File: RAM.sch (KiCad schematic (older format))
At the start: 33 parts, among them IC1 EP4CE10F17, U22 W9751G6KB

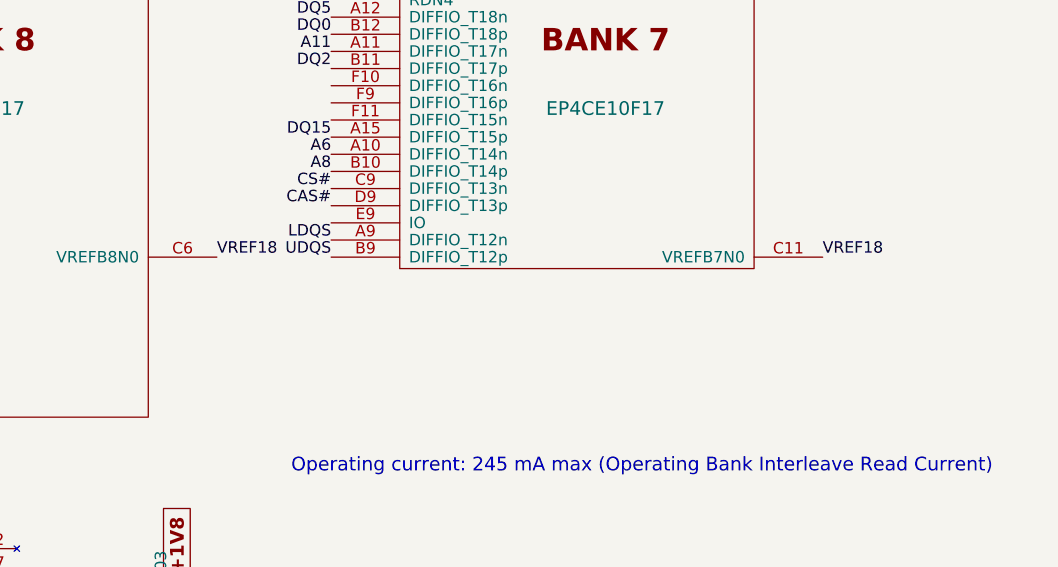
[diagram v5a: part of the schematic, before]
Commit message: More caps for VREF
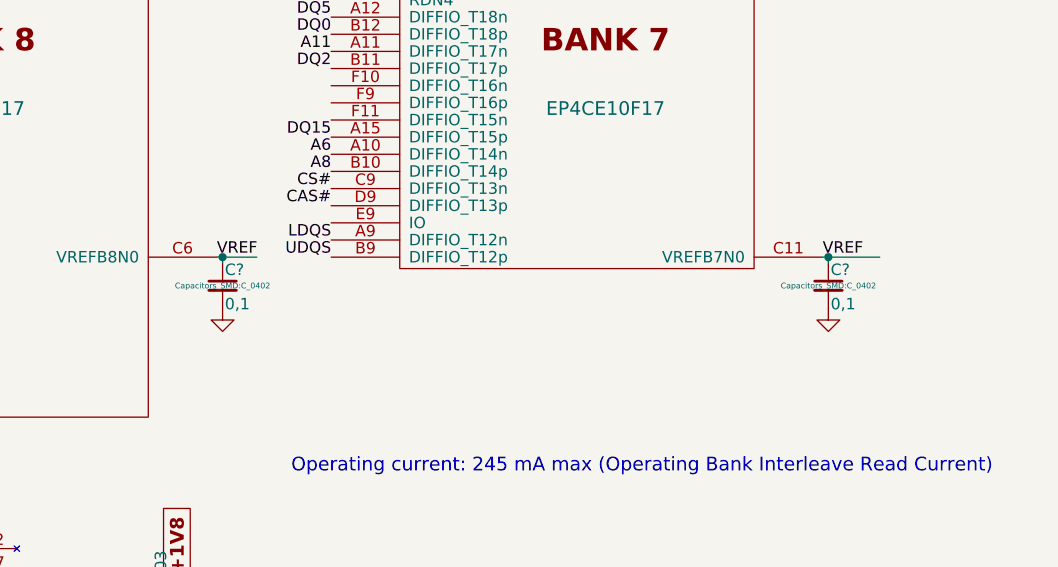
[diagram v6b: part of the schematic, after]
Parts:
- added C? (x2): 0,1, Capacitors_SMD:C_0402, symbol C_Small
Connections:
- net labels removed: VREF18
- wire segments 168 -> 172
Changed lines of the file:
@@
 NoConn ~ 2700 6575
 Text Label 8775 2600 0    50   ~ 0
-VREF18
+VREF
 $Comp
 L C_Small C105
@@
 Connection ~ 5950 4475
 Text Label 6125 2600 0    50   ~ 0
-VREF18
+VREF
+$Comp
+L C_Small C?
+U 1 1 588F9339
+P 6150 2725
+F 0 "C?" H 6160 2795 50  0000 L CNN
+F 1 "0,1" H 6160 2645 50  0000 L CNN
+F 2 "Capacitors_SMD:C_0402" H 6150 2725 25  0000 C CNN
+F 3 "" H 6150 2725 50  0000 C CNN
+	1    6150 2725
+	1    0    0    -1
+$EndComp
+$Comp
+L GND #PWR?
+U 1 1 588F9480
+P 6150 2825
+F 0 "#PWR?" H 6150 2575 50  0001 C CNN
+F 1 "GND" H 6150 2675 50  0001 C CNN
+F 2 "" H 6150 2825 50  0000 C CNN
+F 3 "" H 6150 2825 50  0000 C CNN
+	1    6150 2825
+	1    0    0    -1
+$EndComp
+Wire Wire Line
+	6150 2625 6150 2600
+Wire Wire Line
+	6125 2600 6300 2600
+Connection ~ 6150 2600
+$Comp
+L C_Small C?
+U 1 1 588F9FB7
+P 8800 2725
+F 0 "C?" H 8810 2795 50  0000 L CNN
+F 1 "0,1" H 8810 2645 50  0000 L CNN
+F 2 "Capacitors_SMD:C_0402" H 8800 2725 25  0000 C CNN
+F 3 "" H 8800 2725 50  0000 C CNN
+	1    8800 2725
+	1    0    0    -1
+$EndComp
+$Comp
+L GND #PWR?
+U 1 1 588FA0B7
+P 8800 2825
+F 0 "#PWR?" H 8800 2575 50  0001 C CNN
+F 1 "GND" H 8800 2675 50  0001 C CNN
+F 2 "" H 8800 2825 50  0000 C CNN
+F 3 "" H 8800 2825 50  0000 C CNN
+	1    8800 2825
+	1    0    0    -1
+$EndComp
+Wire Wire Line
+	8775 2600 9025 2600
+Wire Wire Line
+	8800 2625 8800 2600
+Connection ~ 8800 2600
 $EndSCHEMATC

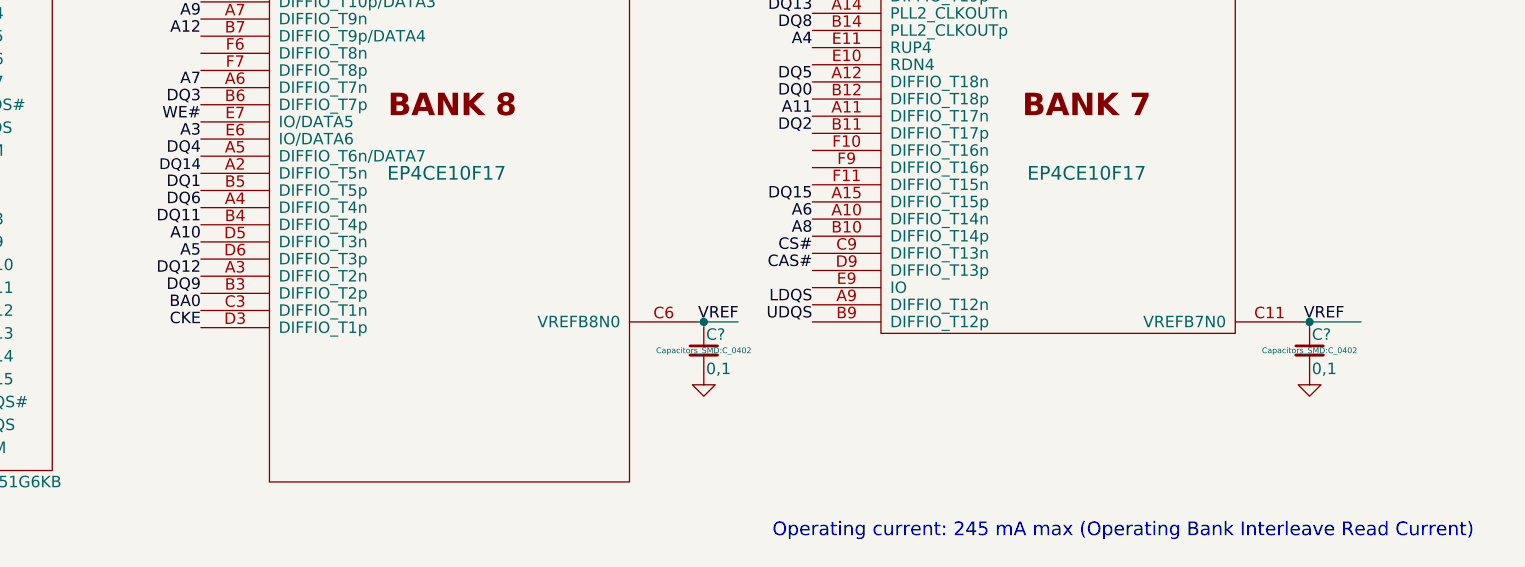
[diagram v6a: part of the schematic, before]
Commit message: More caps for VREF-2
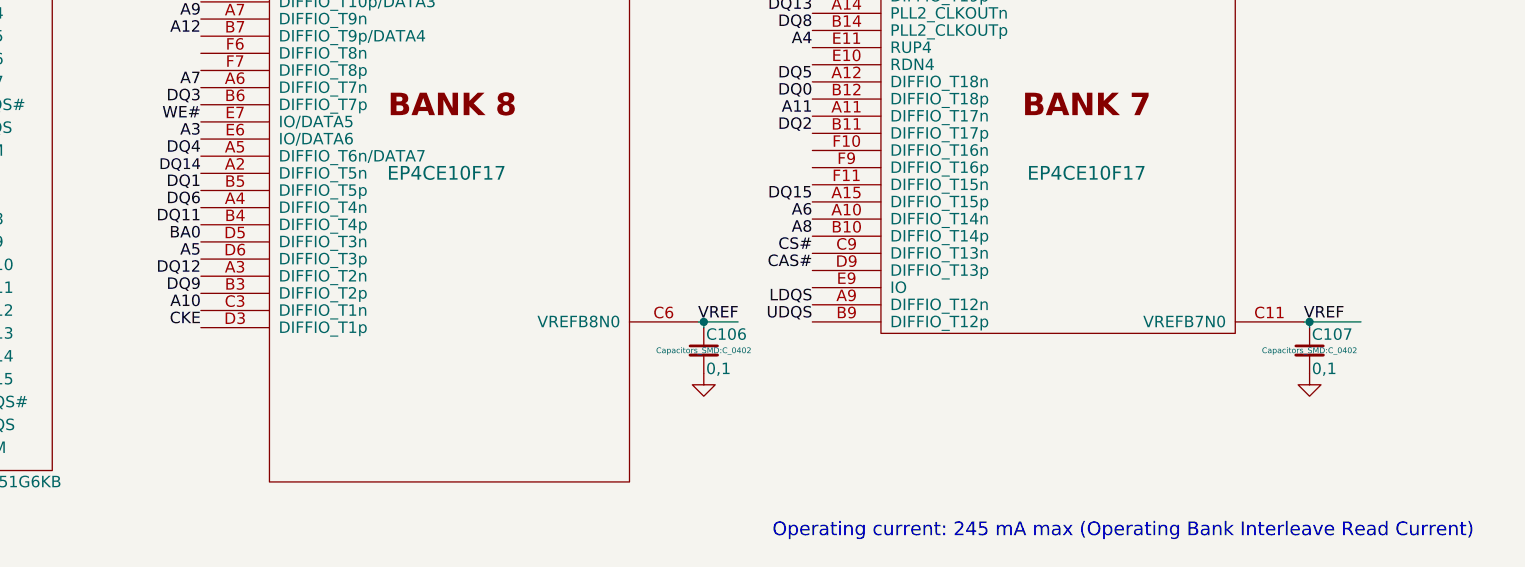
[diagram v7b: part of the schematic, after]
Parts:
- gave numbers to parts that had none: 2
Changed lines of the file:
@@
 CKE
 Text Label 3950 2550 2    50   ~ 0
-BA0
-Text Label 3950 2250 2    50   ~ 0
 A10
 Text Label 3950 1800 2    50   ~ 0
@@
 +1V8
 $Comp
-L GND #PWR134
+L GND #PWR135
 U 1 1 5883C563
 P 6950 5300
-F 0 "#PWR134" H 6950 5050 50  0001 C CNN
+F 0 "#PWR135" H 6950 5050 50  0001 C CNN
 F 1 "GND" H 6950 5150 50  0001 C CNN
 F 2 "" H 6950 5300 50  0000 C CNN
@@
 $EndComp
 $Comp
-L GND #PWR135
+L GND #PWR136
 U 1 1 5883EF35
 P 6950 5925
-F 0 "#PWR135" H 6950 5675 50  0001 C CNN
+F 0 "#PWR136" H 6950 5675 50  0001 C CNN
 F 1 "GND" H 6950 5775 50  0001 C CNN
 F 2 "" H 6950 5925 50  0000 C CNN
@@
 Connection ~ 6950 4850
 $Comp
-L GND #PWR136
+L GND #PWR137
 U 1 1 588A8459
 P 7800 4800
-F 0 "#PWR136" H 7800 4550 50  0001 C CNN
+F 0 "#PWR137" H 7800 4550 50  0001 C CNN
 F 1 "GND" H 7800 4650 50  0001 C CNN
 F 2 "" H 7800 4800 50  0000 C CNN
@@
 VREF
 $Comp
-L C_Small C?
+L C_Small C106
 U 1 1 588F9339
 P 6150 2725
-F 0 "C?" H 6160 2795 50  0000 L CNN
+F 0 "C106" H 6160 2795 50  0000 L CNN
 F 1 "0,1" H 6160 2645 50  0000 L CNN
 F 2 "Capacitors_SMD:C_0402" H 6150 2725 25  0000 C CNN
@@
 $EndComp
 $Comp
-L GND #PWR?
+L GND #PWR134
 U 1 1 588F9480
 P 6150 2825
-F 0 "#PWR?" H 6150 2575 50  0001 C CNN
+F 0 "#PWR134" H 6150 2575 50  0001 C CNN
 F 1 "GND" H 6150 2675 50  0001 C CNN
 F 2 "" H 6150 2825 50  0000 C CNN
@@
 Connection ~ 6150 2600
 $Comp
-L C_Small C?
+L C_Small C107
 U 1 1 588F9FB7
 P 8800 2725
-F 0 "C?" H 8810 2795 50  0000 L CNN
+F 0 "C107" H 8810 2795 50  0000 L CNN
 F 1 "0,1" H 8810 2645 50  0000 L CNN
 F 2 "Capacitors_SMD:C_0402" H 8800 2725 25  0000 C CNN
@@
 $EndComp
 $Comp
-L GND #PWR?
+L GND #PWR138
 U 1 1 588FA0B7
 P 8800 2825
-F 0 "#PWR?" H 8800 2575 50  0001 C CNN
+F 0 "#PWR138" H 8800 2575 50  0001 C CNN
 F 1 "GND" H 8800 2675 50  0001 C CNN
 F 2 "" H 8800 2825 50  0000 C CNN
@@
 	8800 2625 8800 2600
 Connection ~ 8800 2600
+Text Label 3950 2250 2    50   ~ 0
+BA0
 $EndSCHEMATC
